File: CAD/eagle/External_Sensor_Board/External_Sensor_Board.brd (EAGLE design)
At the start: 50.8 x 43.4 mm, 13 parts, among them J1 SFW15R_FFC, J2 J30J-25, U1 MAX31725MTA+, U2 HSCMNNN1.6BAAA3, U3 P82B715

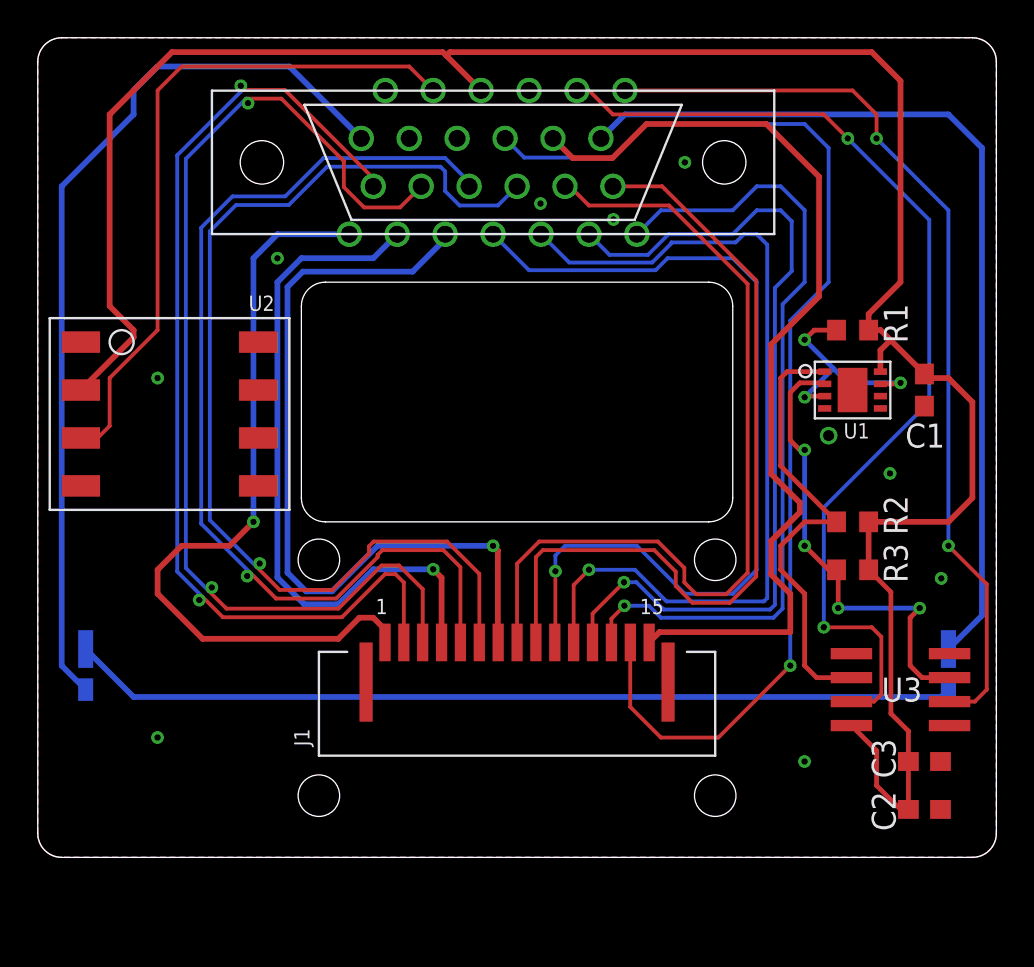
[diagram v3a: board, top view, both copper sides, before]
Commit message: Added bias voltage route to external board
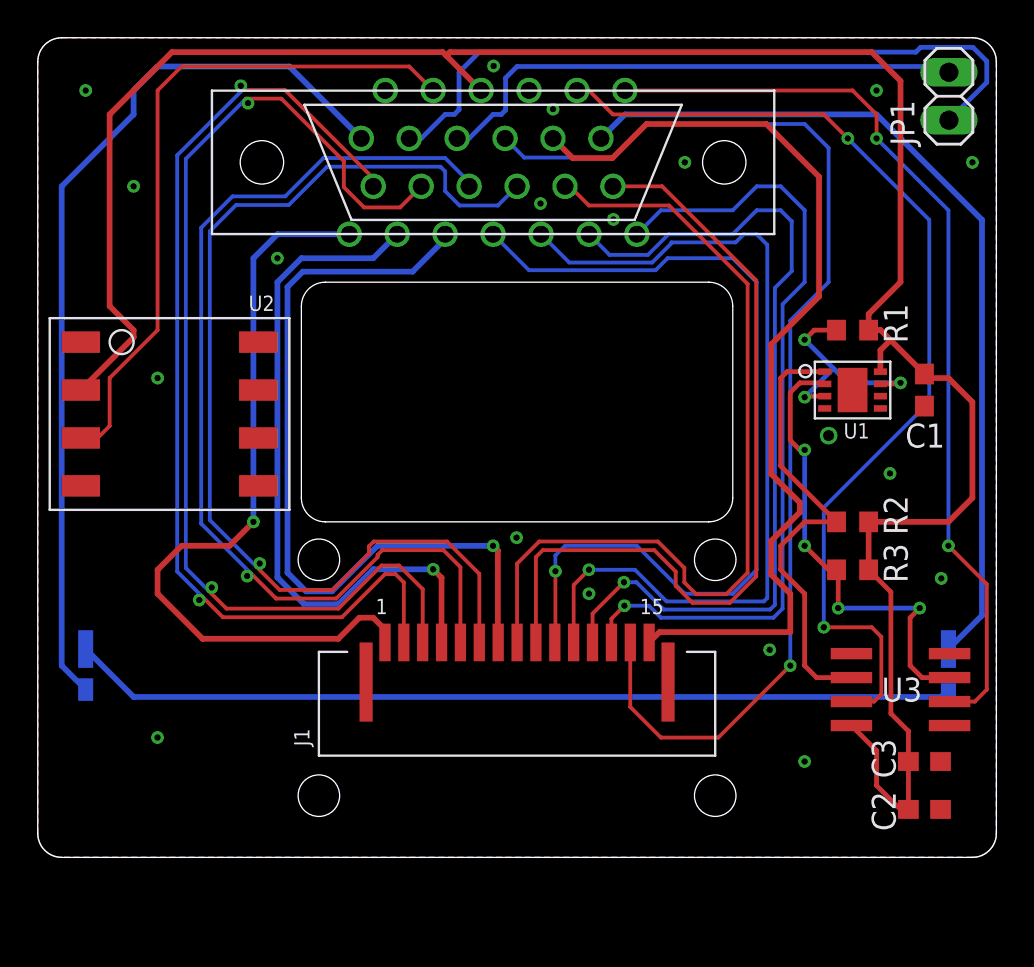
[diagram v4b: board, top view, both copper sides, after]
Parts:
- added JP1: (no value), pinhead:1X02
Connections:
- new net BIAS_28V: J2.16, JP1.1
- new net BIAS_GND: J2.18, JP1.2
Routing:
- net BIAS_28V: track 0.00 -> 38.0 mm
- net BIAS_GND: track 0.00 -> 28.8 mm
- net LED_OUT: track 48.7 -> 46.5 mm
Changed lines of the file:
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@@
 </element>
 <element name="J2" library="CM_J30J" package="ZKN-25" value="J30J-25" x="24.13" y="40.64" smashed="yes"/>
+<element name="JP1" library="pinhead" package="1X02" value="" x="48.2854" y="44.1452" rot="R90"/>
 </elements>
 <signals>
@@
 <via x="6.35" y="10.16" extent="1-16" drill="0.3302"/>
 <via x="40.64" y="8.89" extent="1-16" drill="0.3302"/>
+<via x="44.45" y="44.45" extent="1-16" drill="0.3302"/>
+<via x="49.53" y="40.64" extent="1-16" drill="0.3302"/>
+<via x="24.1554" y="45.7454" extent="1-16" drill="0.3302"/>
+<via x="27.305" y="43.4594" extent="1-16" drill="0.3302"/>
+<via x="25.3746" y="20.7518" extent="1-16" drill="0.3302"/>
+<via x="38.7858" y="14.8082" extent="1-16" drill="0.3302"/>
+<via x="29.21" y="17.78" extent="1-16" drill="0.3302"/>
+<via x="5.08" y="39.37" extent="1-16" drill="0.3302"/>
+<via x="2.54" y="44.45" extent="1-16" drill="0.3302"/>
 </signal>
 <signal name="SDA">
@@
 <contactref element="J2" pad="24"/>
 <wire x1="48.26" y1="14.85" x2="50.038" y2="16.628" width="0.3048" layer="16"/>
-<wire x1="50.038" y1="16.628" x2="50.038" y2="41.402" width="0.3048" layer="16"/>
-<wire x1="50.038" y1="41.402" x2="48.26" y2="43.18" width="0.3048" layer="16"/>
-<wire x1="48.26" y1="43.18" x2="31.115" y2="43.18" width="0.3048" layer="16"/>
+<wire x1="50.038" y1="16.628" x2="50.038" y2="37.592" width="0.3048" layer="16"/>
+<wire x1="44.45" y1="43.18" x2="31.115" y2="43.18" width="0.3048" layer="16"/>
 <wire x1="31.115" y1="43.18" x2="29.845" y2="41.91" width="0.3048" layer="16"/>
+<wire x1="44.45" y1="43.18" x2="50.038" y2="37.592" width="0.3048" layer="16"/>
 </signal>
 <signal name="N$2">
@@
 <wire x1="43.18" y1="44.45" x2="31.115" y2="44.45" width="0.2032" layer="1"/>
 </signal>
+<signal name="BIAS_28V">
+<contactref element="JP1" pad="1"/>
+<contactref element="J2" pad="16"/>
+<wire x1="19.685" y1="41.91" x2="20.32" y2="41.91" width="0.254" layer="16"/>
+<wire x1="20.32" y1="41.91" x2="21.59" y2="43.18" width="0.254" layer="16"/>
+<wire x1="21.59" y1="43.18" x2="22.0726" y2="43.18" width="0.254" layer="16"/>
+<wire x1="22.0726" y1="43.18" x2="22.3266" y2="43.434" width="0.254" layer="16"/>
+<wire x1="22.3266" y1="43.434" x2="22.3266" y2="45.4152" width="0.254" layer="16"/>
+<wire x1="22.3266" y1="45.4152" x2="23.3934" y2="46.482" width="0.254" layer="16"/>
+<wire x1="23.3934" y1="46.482" x2="46.5328" y2="46.482" width="0.254" layer="16"/>
+<wire x1="46.5328" y1="46.482" x2="46.7868" y2="46.736" width="0.254" layer="16"/>
+<wire x1="46.7868" y1="46.736" x2="49.5554" y2="46.736" width="0.254" layer="16"/>
+<wire x1="49.5554" y1="46.736" x2="50.292" y2="45.9994" width="0.254" layer="16"/>
+<wire x1="50.292" y1="45.9994" x2="50.292" y2="44.8818" width="0.254" layer="16"/>
+<wire x1="50.292" y1="44.8818" x2="48.2854" y2="42.8752" width="0.254" layer="16"/>
+</signal>
+<signal name="BIAS_GND">
+<contactref element="JP1" pad="2"/>
+<contactref element="J2" pad="18"/>
+<wire x1="22.225" y1="41.91" x2="22.86" y2="41.91" width="0.254" layer="16"/>
+<wire x1="22.86" y1="41.91" x2="24.13" y2="43.18" width="0.254" layer="16"/>
+<wire x1="24.13" y1="43.18" x2="24.5618" y2="43.18" width="0.254" layer="16"/>
+<wire x1="24.5618" y1="43.18" x2="24.7904" y2="43.4086" width="0.254" layer="16"/>
+<wire x1="24.7904" y1="43.4086" x2="24.7904" y2="45.1104" width="0.254" layer="16"/>
+<wire x1="24.7904" y1="45.1104" x2="25.4" y2="45.72" width="0.254" layer="16"/>
+<wire x1="25.4" y1="45.72" x2="47.9806" y2="45.72" width="0.254" layer="16"/>
+<wire x1="47.9806" y1="45.72" x2="48.2854" y2="45.4152" width="0.254" layer="16"/>
+</signal>
 </signals>

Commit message: Better differential pair routing.
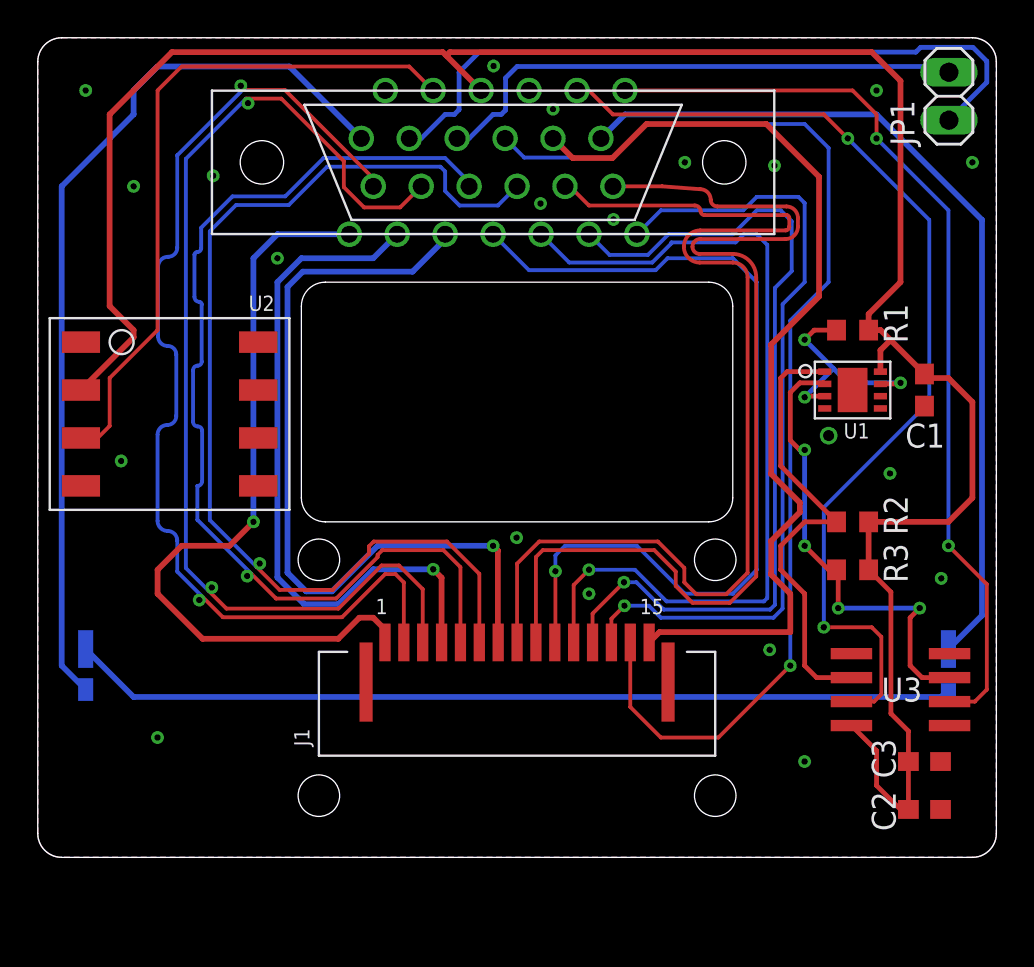
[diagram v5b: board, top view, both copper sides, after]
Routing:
- net CAM_C_N: track 46.1 -> 57.7 mm
- net CAM_C_P: track 43.9 -> 55.4 mm
- net CAM_D0_N: track 54.5 -> 56.2 mm
- net CAM_D1_N: track 53.5 -> 54.4 mm

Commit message: Began work on pressure sensor library. Realized I specced an inadequate sensor. Specced a better sensor (in the same family). Changed external sensor board to compensate.
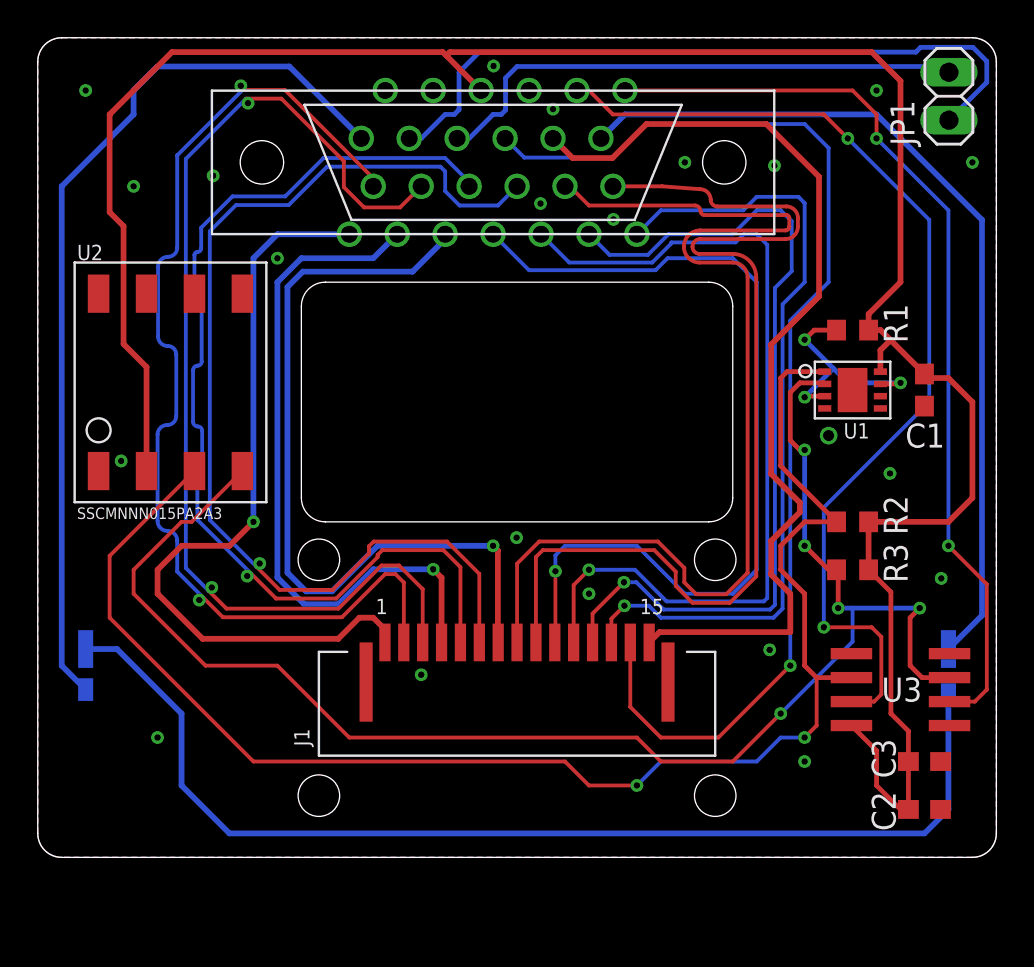
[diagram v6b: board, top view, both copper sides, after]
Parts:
- U2: value HSCMNNN1.6BAAA3 -> SSCMNNN015PA2A3
- moved U2 1.68 mm to (7.04, 29.0), turned to 0 degrees
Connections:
- removed net POUT: J2.17, U2.3
- net GND: now also U2.1; no longer U2.4
- net SCL: now also U2.4
- net SDA: now also U2.3
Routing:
- net SCL: track 24.9 -> 80.3 mm, vias 4 -> 5
- net SDA: track 24.4 -> 79.1 mm, vias 0 -> 2
- net POUT: track 36.3 -> 0.00 mm
- net N$2: track 46.9 -> 58.9 mm
- net +3V3: track 119.0 -> 122.4 mm
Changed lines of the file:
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@@
 <attribute name="NAME" x="42.704" y="26.007" size="0.8128" layer="25"/>
-</element>
-<element name="U2" library="NR_IC" package="HSC-SMT-8" value="HSCMNNN1.6BAAA3" x="6.985" y="27.305" smashed="yes" rot="R270">
-<attribute name="NAME" x="11.176" y="32.766" size="0.8128" layer="25"/>
 </element>
 <element name="U3" library="CM_IC" package="SO8" value="P82B715" x="45.72" y="12.7" smashed="yes" rot="R90">
@@
 <element name="J2" library="CM_J30J" package="ZKN-25" value="J30J-25" x="24.13" y="40.64" smashed="yes"/>
 <element name="JP1" library="pinhead" package="1X02" value="" x="48.2854" y="44.1452" rot="R90"/>
+<element name="U2" library="NR_IC" package="HSC-SMT-8" value="SSCMNNN015PA2A3" x="7.0358" y="28.9814"/>
 </elements>
 <signals>
@@
 <contactref element="U1" pad="8"/>
 <contactref element="R1" pad="1"/>
-<contactref element="U2" pad="2"/>
 <contactref element="R2" pad="1"/>
 <contactref element="R3" pad="1"/>
@@
 <wire x1="21.844" y1="46.482" x2="21.6535" y2="46.2915" width="0.3048" layer="1"/>
 <wire x1="7.112" y1="46.482" x2="3.81" y2="43.18" width="0.3048" layer="1"/>
-<wire x1="3.81" y1="43.18" x2="3.81" y2="33.02" width="0.3048" layer="1"/>
-<wire x1="3.81" y1="33.02" x2="5.08" y2="31.75" width="0.3048" layer="1"/>
-<wire x1="5.08" y1="31.75" x2="5.08" y2="31.369" width="0.3048" layer="1"/>
-<wire x1="5.08" y1="31.369" x2="2.286" y2="28.575" width="0.3048" layer="1"/>
+<contactref element="U2" pad="2"/>
+<wire x1="5.7658" y1="24.2824" x2="5.7658" y2="29.7942" width="0.3048" layer="1"/>
+<wire x1="5.7658" y1="29.7942" x2="4.5466" y2="31.0134" width="0.3048" layer="1"/>
+<wire x1="4.5466" y1="31.0134" x2="4.5466" y2="37.2618" width="0.3048" layer="1"/>
+<wire x1="4.5466" y1="37.2618" x2="3.81" y2="37.9984" width="0.3048" layer="1"/>
+<wire x1="3.81" y1="37.9984" x2="3.81" y2="43.18" width="0.3048" layer="1"/>
 </signal>
 <signal name="GND">
@@
 <contactref element="U1" pad="6"/>
 <contactref element="U1" pad="5"/>
-<contactref element="U2" pad="4"/>
 <via x="41.91" y="26.162" extent="1-16" drill="0.5842"/>
 <contactref element="U3" pad="4"/>
@@
 <via x="9.2964" y="39.9288" extent="1-16" drill="0.3302"/>
 <via x="39.0398" y="40.4622" extent="1-16" drill="0.3302"/>
+<contactref element="U2" pad="1"/>
+<via x="20.32" y="13.4874" extent="1-16" drill="0.3302"/>
 </signal>
 <signal name="SDA">
@@
 <wire x1="39.37" y1="20.32" x2="40.64" y2="21.59" width="0.254" layer="1"/>
 <wire x1="40.64" y1="21.59" x2="42.33" y2="21.59" width="0.254" layer="1"/>
+<contactref element="U2" pad="3"/>
+<wire x1="8.3058" y1="24.2824" x2="3.81" y2="19.7866" width="0.2032" layer="1"/>
+<wire x1="3.81" y1="19.7866" x2="3.81" y2="16.51" width="0.2032" layer="1"/>
+<wire x1="3.81" y1="16.51" x2="11.43" y2="8.89" width="0.2032" layer="1"/>
+<wire x1="11.43" y1="8.89" x2="27.94" y2="8.89" width="0.2032" layer="1"/>
+<wire x1="27.94" y1="8.89" x2="29.21" y2="7.62" width="0.2032" layer="1"/>
+<wire x1="29.21" y1="7.62" x2="31.75" y2="7.62" width="0.2032" layer="1"/>
+<via x="31.75" y="7.62" extent="1-16" drill="0.3302"/>
+<wire x1="31.75" y1="7.62" x2="33.02" y2="8.89" width="0.2032" layer="16"/>
+<wire x1="33.02" y1="8.89" x2="38.1" y2="8.89" width="0.2032" layer="16"/>
+<wire x1="38.1" y1="8.89" x2="39.37" y2="10.16" width="0.2032" layer="16"/>
+<wire x1="39.37" y1="10.16" x2="40.64" y2="10.16" width="0.2032" layer="16"/>
+<via x="40.64" y="10.16" extent="1-16" drill="0.3302"/>
+<wire x1="40.64" y1="10.16" x2="41.275" y2="10.795" width="0.2032" layer="1"/>
+<wire x1="41.275" y1="10.795" x2="41.275" y2="13.335" width="0.2032" layer="1"/>
 </signal>
 <signal name="SCL">
@@
 <wire x1="46.228" y1="16.51" x2="46.736" y2="17.018" width="0.254" layer="1"/>
 <via x="46.736" y="17.018" extent="1-16" drill="0.3302"/>
-<wire x1="46.736" y1="17.018" x2="42.418" y2="17.018" width="0.254" layer="16"/>
+<wire x1="46.736" y1="17.018" x2="43.18" y2="17.018" width="0.254" layer="16"/>
 <via x="42.418" y="17.018" extent="1-16" drill="0.3302"/>
+<wire x1="43.18" y1="17.018" x2="42.418" y2="17.018" width="0.254" layer="16"/>
 <wire x1="42.418" y1="17.018" x2="42.418" y2="18.962" width="0.254" layer="1"/>
 <wire x1="42.418" y1="18.962" x2="42.33" y2="19.05" width="0.254" layer="1"/>
+<contactref element="U2" pad="4"/>
+<wire x1="10.8458" y1="24.2824" x2="8.1534" y2="21.59" width="0.2032" layer="1"/>
+<wire x1="8.1534" y1="21.59" x2="7.62" y2="21.59" width="0.2032" layer="1"/>
+<wire x1="7.62" y1="21.59" x2="5.08" y2="19.05" width="0.2032" layer="1"/>
+<wire x1="5.08" y1="19.05" x2="5.08" y2="17.78" width="0.2032" layer="1"/>
+<wire x1="5.08" y1="17.78" x2="8.89" y2="13.97" width="0.2032" layer="1"/>
+<wire x1="8.89" y1="13.97" x2="12.7" y2="13.97" width="0.2032" layer="1"/>
+<wire x1="12.7" y1="13.97" x2="16.51" y2="10.16" width="0.2032" layer="1"/>
+<wire x1="16.51" y1="10.16" x2="31.75" y2="10.16" width="0.2032" layer="1"/>
+<wire x1="31.75" y1="10.16" x2="33.02" y2="8.89" width="0.2032" layer="1"/>
+<wire x1="33.02" y1="8.89" x2="36.83" y2="8.89" width="0.2032" layer="1"/>
+<wire x1="36.83" y1="8.89" x2="39.37" y2="11.43" width="0.2032" layer="1"/>
+<via x="39.37" y="11.43" extent="1-16" drill="0.3302"/>
+<wire x1="39.37" y1="11.43" x2="43.18" y2="15.24" width="0.2032" layer="16"/>
+<wire x1="43.18" y1="15.24" x2="43.18" y2="17.018" width="0.2032" layer="16"/>
 </signal>
 <signal name="N$1">
@@
 <via x="40.64" y="28.194" extent="1-16" drill="0.3302"/>
 <wire x1="40.64" y1="28.194" x2="42.164" y2="29.718" width="0.254" layer="16"/>
-</signal>
-<signal name="POUT">
-<contactref element="U2" pad="3"/>
-<contactref element="J2" pad="17"/>
-<wire x1="2.286" y1="26.035" x2="3.175" y2="26.035" width="0.2032" layer="1"/>
-<wire x1="3.175" y1="26.035" x2="3.81" y2="26.67" width="0.2032" layer="1"/>
-<wire x1="3.81" y1="26.67" x2="3.81" y2="29.21" width="0.2032" layer="1"/>
-<wire x1="3.81" y1="29.21" x2="6.35" y2="31.75" width="0.2032" layer="1"/>
-<wire x1="6.35" y1="31.75" x2="6.35" y2="44.45" width="0.2032" layer="1"/>
-<wire x1="6.35" y1="44.45" x2="7.62" y2="45.72" width="0.2032" layer="1"/>
-<wire x1="7.62" y1="45.72" x2="19.685" y2="45.72" width="0.2032" layer="1"/>
-<wire x1="19.685" y1="45.72" x2="20.955" y2="44.45" width="0.2032" layer="1"/>
 </signal>
 <signal name="CAM_3V3">
@@
 <contactref element="LED1" pad="1"/>
 <contactref element="LED2" pad="2"/>
-<wire x1="2.54" y1="14.85" x2="5.08" y2="12.31" width="0.3048" layer="16"/>
-<wire x1="5.08" y1="12.31" x2="47.87" y2="12.31" width="0.3048" layer="16"/>
-<wire x1="47.87" y1="12.31" x2="48.26" y2="12.7" width="0.3048" layer="16"/>
+<wire x1="2.54" y1="14.85" x2="4.2" y2="14.85" width="0.3048" layer="16"/>
+<wire x1="4.2" y1="14.85" x2="7.62" y2="11.43" width="0.3048" layer="16"/>
+<wire x1="7.62" y1="11.43" x2="7.62" y2="7.62" width="0.3048" layer="16"/>
+<wire x1="7.62" y1="7.62" x2="10.16" y2="5.08" width="0.3048" layer="16"/>
+<wire x1="10.16" y1="5.08" x2="46.99" y2="5.08" width="0.3048" layer="16"/>
+<wire x1="46.99" y1="5.08" x2="48.26" y2="6.35" width="0.3048" layer="16"/>
+<wire x1="48.26" y1="6.35" x2="48.26" y2="12.7" width="0.3048" layer="16"/>
 </signal>
 <signal name="CAM_GND1">
